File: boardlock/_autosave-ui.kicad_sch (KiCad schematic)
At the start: 31 parts, among them J6 USB_C_Receptacle_USB2.0, Q5 DTC124X, Q6 DTC124X, Q7 DTC124X, SW1 SW_Push, SW2 SW_Push, SW3 TL3300DF160Q, SW5 TL3300DF160Q

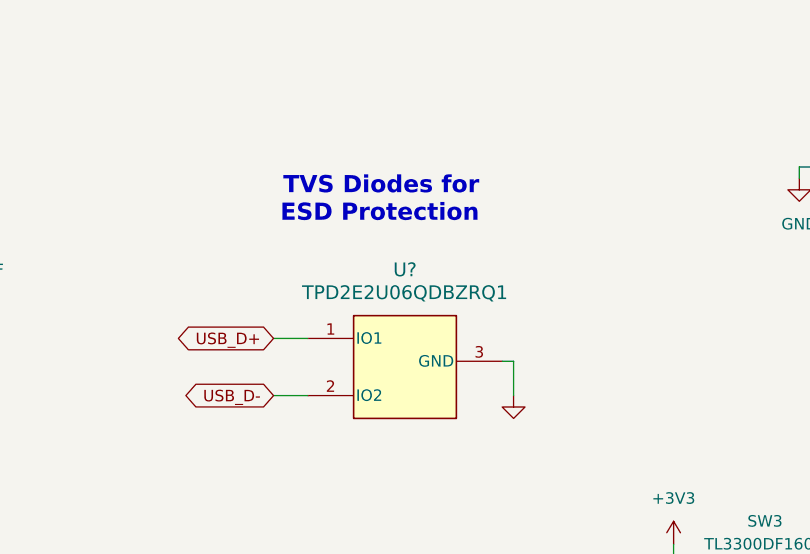
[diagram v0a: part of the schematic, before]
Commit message: replaced TVS footprint and rerouted USB
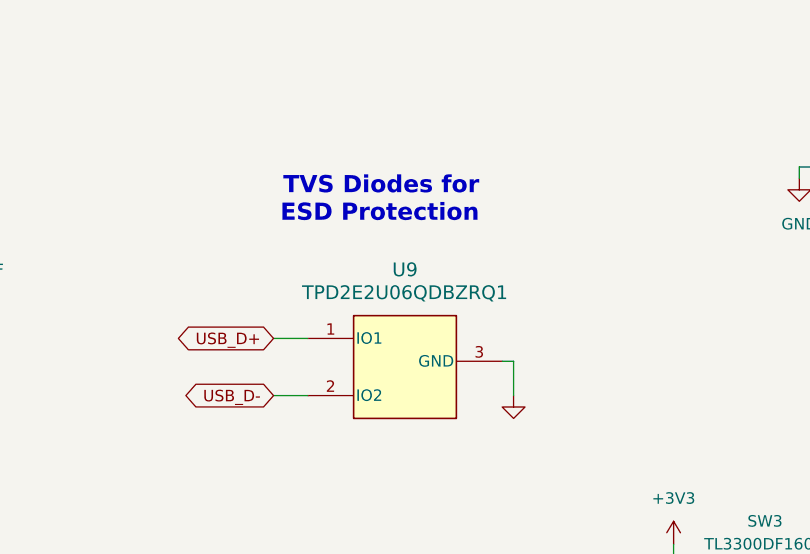
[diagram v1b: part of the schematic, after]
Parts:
- gave numbers to parts that had none: 1
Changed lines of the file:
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@@
   (symbol (lib_id "TPD2E2U06QDBZRQ1:TPD2E2U06QDBZRQ1") (at 142.24 62.23 0) (unit 1)
     (in_bom yes) (on_board yes) (dnp no) (fields_autoplaced)
-    (property "Reference" "U?" (at 142.875 52.07 0)
+    (property "Reference" "U9" (at 142.875 52.07 0)
       (effects (font (size 1.524 1.524)))
     )
@@
       (project "boardlock"
         (path "/e1fc29ce-837e-4062-84d8-c7e423f9eab9/c1e95beb-a482-4f8e-b13b-3641abb17f9b"
-          (reference "U?") (unit 1)
+          (reference "U9") (unit 1)
         )
       )
